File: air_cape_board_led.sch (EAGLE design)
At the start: 10 parts

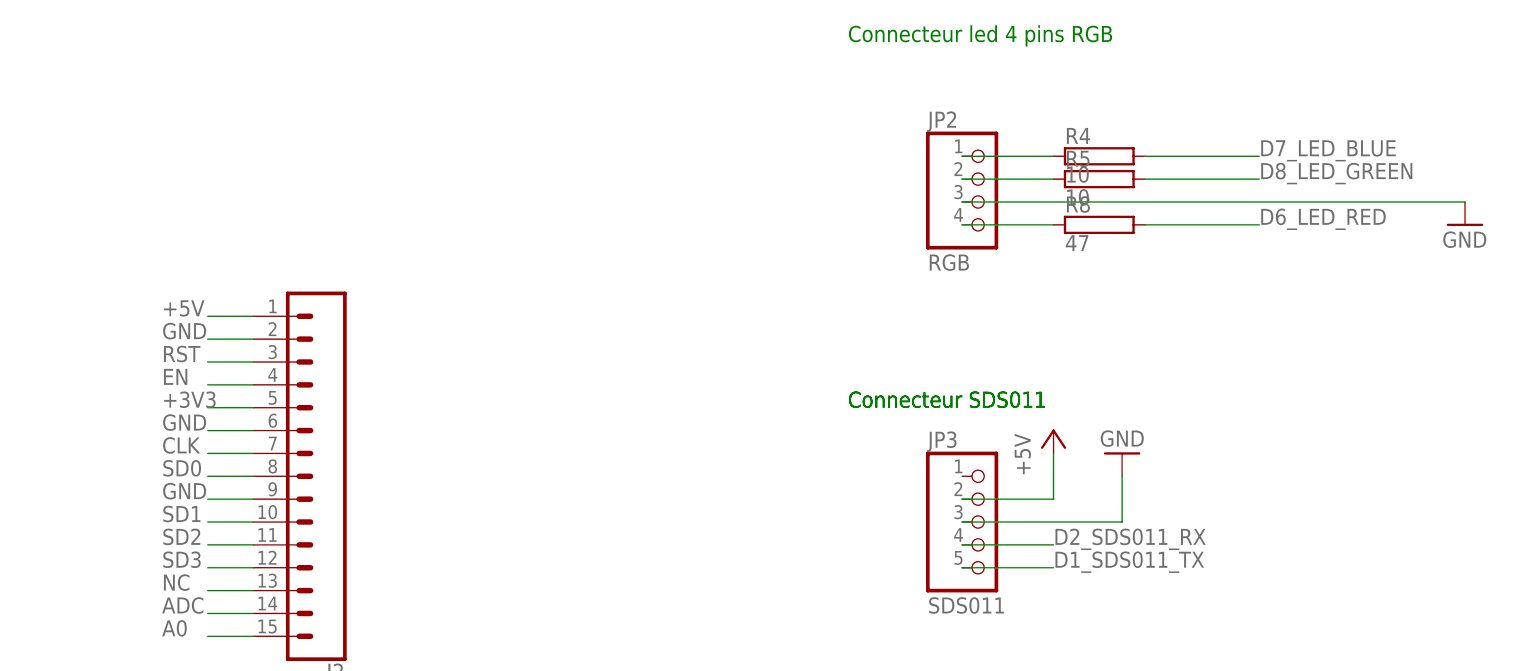
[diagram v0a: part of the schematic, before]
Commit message: Fix issue with led power supply
- Should be VDD instead of GND
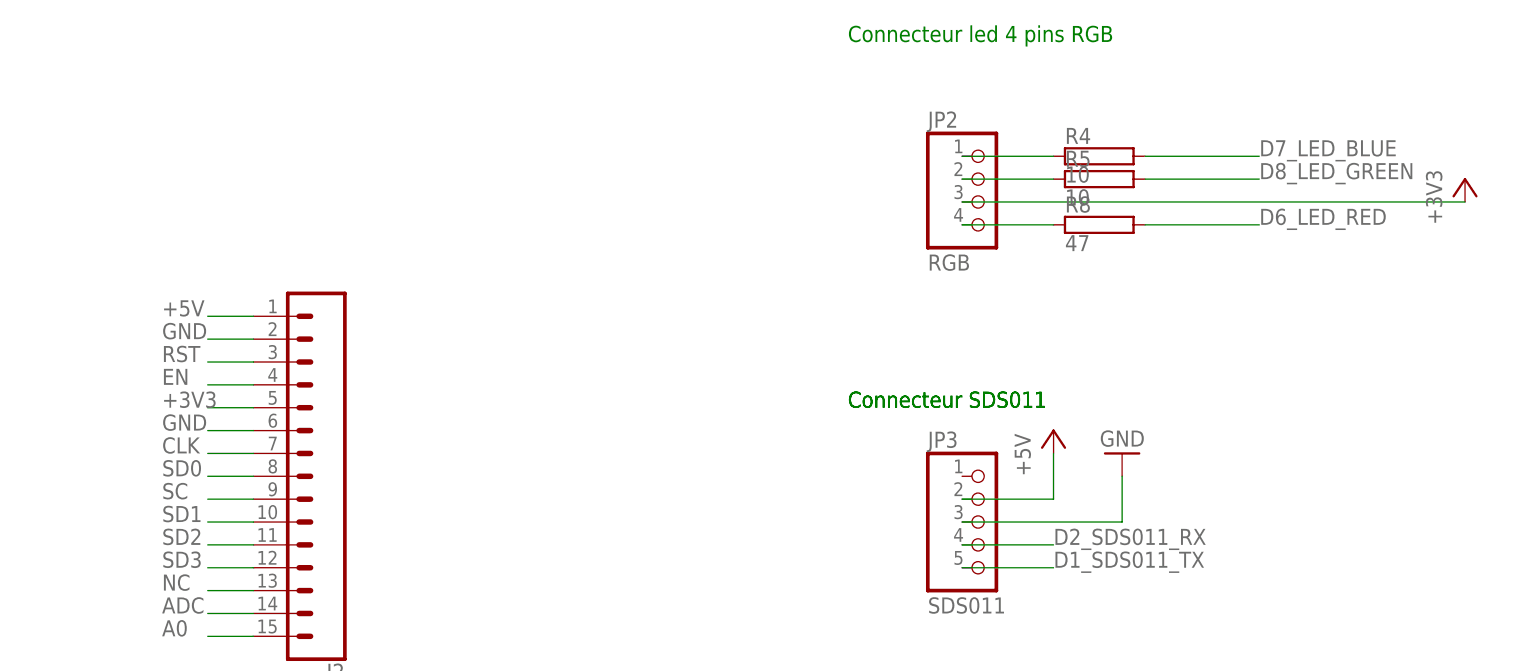
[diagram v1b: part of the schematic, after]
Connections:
- new net SC: J2.9
- net +3V3: now also JP2.3
- net GND: no longer J2.9, JP2.3
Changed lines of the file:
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@@
 <grid distance="0.1" unitdist="inch" unit="inch" style="lines" multiple="1" display="no" altdistance="0.01" altunitdist="inch" altunit="inch"/>
 <layers>
-<layer number="1" name="Top" color="4" fill="1" visible="yes" active="no"/>
-<layer number="16" name="Bottom" color="1" fill="1" visible="yes" active="no"/>
-<layer number="17" name="Pads" color="2" fill="1" visible="yes" active="no"/>
-<layer number="18" name="Vias" color="2" fill="1" visible="yes" active="no"/>
-<layer number="19" name="Unrouted" color="6" fill="1" visible="yes" active="no"/>
-<layer number="20" name="Dimension" color="24" fill="1" visible="yes" active="no"/>
-<layer number="21" name="tPlace" color="7" fill="1" visible="yes" active="no"/>
-<layer number="22" name="bPlace" color="7" fill="1" visible="yes" active="no"/>
-<layer number="23" name="tOrigins" color="15" fill="1" visible="yes" active="no"/>
-<layer number="24" name="bOrigins" color="15" fill="1" visible="yes" active="no"/>
-<layer number="25" name="tNames" color="7" fill="1" visible="yes" active="no"/>
-<layer number="26" name="bNames" color="7" fill="1" visible="yes" active="no"/>
-<layer number="27" name="tValues" color="7" fill="1" visible="yes" active="no"/>
-<layer number="28" name="bValues" color="7" fill="1" visible="yes" active="no"/>
+<layer number="1" name="Top" color="4" fill="1" visible="no" active="no"/>
+<layer number="16" name="Bottom" color="1" fill="1" visible="no" active="no"/>
+<layer number="17" name="Pads" color="2" fill="1" visible="no" active="no"/>
+<layer number="18" name="Vias" color="2" fill="1" visible="no" active="no"/>
+<layer number="19" name="Unrouted" color="6" fill="1" visible="no" active="no"/>
+<layer number="20" name="Dimension" color="24" fill="1" visible="no" active="no"/>
+<layer number="21" name="tPlace" color="7" fill="1" visible="no" active="no"/>
+<layer number="22" name="bPlace" color="7" fill="1" visible="no" active="no"/>
+<layer number="23" name="tOrigins" color="15" fill="1" visible="no" active="no"/>
+<layer number="24" name="bOrigins" color="15" fill="1" visible="no" active="no"/>
+<layer number="25" name="tNames" color="7" fill="1" visible="no" active="no"/>
+<layer number="26" name="bNames" color="7" fill="1" visible="no" active="no"/>
+<layer number="27" name="tValues" color="7" fill="1" visible="no" active="no"/>
+<layer number="28" name="bValues" color="7" fill="1" visible="no" active="no"/>
 <layer number="29" name="tStop" color="7" fill="3" visible="no" active="no"/>
 <layer number="30" name="bStop" color="7" fill="6" visible="no" active="no"/>
@@
 <layer number="35" name="tGlue" color="7" fill="4" visible="no" active="no"/>
 <layer number="36" name="bGlue" color="7" fill="5" visible="no" active="no"/>
-<layer number="37" name="tTest" color="7" fill="1" visible="yes" active="no"/>
-<layer number="38" name="bTest" color="7" fill="1" visible="yes" active="no"/>
+<layer number="37" name="tTest" color="7" fill="1" visible="no" active="no"/>
+<layer number="38" name="bTest" color="7" fill="1" visible="no" active="no"/>
 <layer number="39" name="tKeepout" color="4" fill="11" visible="no" active="no"/>
 <layer number="40" name="bKeepout" color="1" fill="11" visible="no" active="no"/>
@@
 <layer number="44" name="Drills" color="7" fill="1" visible="no" active="no"/>
 <layer number="45" name="Holes" color="7" fill="1" visible="no" active="no"/>
-<layer number="46" name="Milling" color="3" fill="1" visible="yes" active="no"/>
-<layer number="47" name="Measures" color="7" fill="1" visible="yes" active="no"/>
-<layer number="48" name="Document" color="7" fill="1" visible="yes" active="no"/>
-<layer number="49" name="Reference" color="7" fill="1" visible="yes" active="no"/>
-<layer number="50" name="dxf" color="7" fill="1" visible="yes" active="no"/>
-<layer number="51" name="tDocu" color="7" fill="1" visible="yes" active="no"/>
-<layer number="52" name="bDocu" color="7" fill="1" visible="yes" active="no"/>
-<layer number="53" name="tGND_GNDA" color="7" fill="9" visible="yes" active="no"/>
-<layer number="54" name="bGND_GNDA" color="1" fill="9" visible="yes" active="no"/>
-<layer number="56" name="wert" color="7" fill="1" visible="yes" active="no"/>
-<layer number="57" name="tCAD" color="7" fill="1" visible="yes" active="no"/>
-<layer number="59" name="tCarbon" color="7" fill="1" visible="yes" active="no"/>
-<layer number="60" name="bCarbon" color="7" fill="1" visible="yes" active="no"/>
+<layer number="46" name="Milling" color="3" fill="1" visible="no" active="no"/>
+<layer number="47" name="Measures" color="7" fill="1" visible="no" active="no"/>
+<layer number="48" name="Document" color="7" fill="1" visible="no" active="no"/>
+<layer number="49" name="Reference" color="7" fill="1" visible="no" active="no"/>
+<layer number="50" name="dxf" color="7" fill="1" visible="no" active="no"/>
+<layer number="51" name="tDocu" color="7" fill="1" visible="no" active="no"/>
+<layer number="52" name="bDocu" color="7" fill="1" visible="no" active="no"/>
+<layer number="53" name="tGND_GNDA" color="7" fill="9" visible="no" active="no"/>
+<layer number="54" name="bGND_GNDA" color="1" fill="9" visible="no" active="no"/>
+<layer number="56" name="wert" color="7" fill="1" visible="no" active="no"/>
+<layer number="57" name="tCAD" color="7" fill="1" visible="no" active="no"/>
+<layer number="59" name="tCarbon" color="7" fill="1" visible="no" active="no"/>
+<layer number="60" name="bCarbon" color="7" fill="1" visible="no" active="no"/>
 <layer number="88" name="SimResults" color="9" fill="1" visible="yes" active="yes"/>
 <layer number="89" name="SimProbes" color="9" fill="1" visible="yes" active="yes"/>
@@
 <part name="J1" library="SparkFun-Connectors" library_urn="urn:adsk.eagle:library:513" deviceset="CONN_15" device="" package3d_urn="urn:adsk.eagle:package:38190/1"/>
 <part name="J2" library="SparkFun-Connectors" library_urn="urn:adsk.eagle:library:513" deviceset="CONN_15" device="" package3d_urn="urn:adsk.eagle:package:38190/1"/>
-<part name="GND2" library="supply1" library_urn="urn:adsk.eagle:library:371" deviceset="GND" device=""/>
 <part name="GND3" library="supply1" library_urn="urn:adsk.eagle:library:371" deviceset="GND" device=""/>
 <part name="GND5" library="supply1" library_urn="urn:adsk.eagle:library:371" deviceset="GND" device=""/>
@@
 <part name="R9" library="resistor-power" library_urn="urn:adsk.eagle:library:344" deviceset="R" device="RS1/4" package3d_urn="urn:adsk.eagle:package:25167/1" value="5.9k"/>
 <part name="R10" library="resistor-power" library_urn="urn:adsk.eagle:library:344" deviceset="R" device="RS1/4" package3d_urn="urn:adsk.eagle:package:25167/1" value="11.8k"/>
+<part name="+3V5" library="supply1" library_urn="urn:adsk.eagle:library:371" deviceset="+3V3" device=""/>
 </parts>
 <sheets>
@@
 <instance part="J1" gate="G$1" x="60.96" y="106.68"/>
 <instance part="J2" gate="G$1" x="132.08" y="106.68" rot="R180"/>
-<instance part="GND2" gate="1" x="256.54" y="134.62"/>
 <instance part="GND3" gate="1" x="218.44" y="109.22" rot="R180"/>
 <instance part="GND5" gate="1" x="218.44" y="48.26" rot="R180"/>
@@
 <instance part="R9" gate="G$1" x="226.06" y="43.18" rot="R90"/>
 <instance part="R10" gate="G$1" x="241.3" y="43.18" rot="R90"/>
+<instance part="+3V5" gate="G$1" x="256.54" y="139.7"/>
 </instances>
 <busses>
@@
 </segment>
 <segment>
-<pinref part="J2" gate="G$1" pin="9"/>
-<wire x1="121.92" y1="104.14" x2="116.84" y2="104.14" width="0.1524" layer="91"/>
-<label x="111.76" y="104.14" size="1.778" layer="95"/>
-</segment>
-<segment>
-<wire x1="200.66" y1="137.16" x2="256.54" y2="137.16" width="0.1524" layer="91"/>
-<pinref part="GND2" gate="1" pin="GND"/>
-<pinref part="JP2" gate="A" pin="3"/>
-</segment>
-<segment>
 <wire x1="200.66" y1="101.6" x2="218.44" y2="101.6" width="0.1524" layer="91"/>
 <pinref part="GND3" gate="1" pin="GND"/>
@@
 <pinref part="+3V4" gate="G$1" pin="+3V3"/>
 </segment>
+<segment>
+<wire x1="200.66" y1="137.16" x2="256.54" y2="137.16" width="0.1524" layer="91"/>
+<pinref part="JP2" gate="A" pin="3"/>
+<pinref part="+3V5" gate="G$1" pin="+3V3"/>
+</segment>
 </net>
 <net name="+5V" class="0">
@@
 </segment>
 </net>
+<net name="SC" class="0">
+<segment>
+<pinref part="J2" gate="G$1" pin="9"/>
+<wire x1="121.92" y1="104.14" x2="116.84" y2="104.14" width="0.1524" layer="91"/>
+<label x="111.76" y="104.14" size="1.778" layer="95"/>
+</segment>
+</net>
